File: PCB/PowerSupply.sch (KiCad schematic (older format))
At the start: 21 parts, among them U3 MPM54304

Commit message: Add the FPGA symbol
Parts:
- renumbered C12 to C10, C6 to C4, C7 to C5, C8 to C6, C9 to C7, C10 to C8, C11 to C9, U3 to U2
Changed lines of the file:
@@
 $Descr A4 11693 8268
 encoding utf-8
-Sheet 16 17
+Sheet 15 19
 Title "Litter Robot 3 - Power supply"
 Date "2021-03-02"
@@
 $EndDescr
 $Comp
-L LitterRobot:MPM54304 U3
+L LitterRobot:MPM54304 U2
 U 1 1 60487643
 P 5750 3850
-AR Path="/603F1DCE/60487643" Ref="U3"  Part="1"
+AR Path="/603F1DCE/60487643" Ref="U2"  Part="1"
 AR Path="/60624089/60487643" Ref="U?"  Part="1"
-F 0 "U3" H 5750 6381 50  0000 C CNN
+F 0 "U2" H 5750 6381 50  0000 C CNN
 F 1 "MPM54304" H 5750 3850 100 0000 C CNN
 F 2 "LitterRobot:MPS_MPM54304_LGA33_7x7mm" H 6300 6200 50  0001 C CNN
@@
 $EndComp
 $Comp
-L power:+15V #PWR059
+L power:+15V #PWR052
 U 1 1 6049C802
 P 3900 1500
-AR Path="/603F1DCE/6049C802" Ref="#PWR059"  Part="1"
+AR Path="/603F1DCE/6049C802" Ref="#PWR052"  Part="1"
 AR Path="/60624089/6049C802" Ref="#PWR?"  Part="1"
-F 0 "#PWR059" H 3900 1350 50  0001 C CNN
+F 0 "#PWR052" H 3900 1350 50  0001 C CNN
 F 1 "+15V" H 3915 1673 50  0000 C CNN
 F 2 "" H 3900 1500 50  0001 C CNN
@@
 P 4400 1850
 AR Path="/603F20AB/6049E372" Ref="C?"  Part="1"
-AR Path="/603F1DCE/6049E372" Ref="C7"  Part="1"
+AR Path="/603F1DCE/6049E372" Ref="C5"  Part="1"
 AR Path="/60624089/6049E372" Ref="C?"  Part="1"
-F 0 "C7" H 4515 1941 50  0000 L CNN
+F 0 "C5" H 4515 1941 50  0000 L CNN
 F 1 "22µF" H 4515 1850 50  0000 L CNN
 F 2 "Capacitor_SMD:C_0603_1608Metric" H 4438 1700 50  0001 C CNN
@@
 P 3900 1850
 AR Path="/603F20AB/6049F19A" Ref="C?"  Part="1"
-AR Path="/603F1DCE/6049F19A" Ref="C6"  Part="1"
+AR Path="/603F1DCE/6049F19A" Ref="C4"  Part="1"
 AR Path="/60624089/6049F19A" Ref="C?"  Part="1"
-F 0 "C6" H 4015 1941 50  0000 L CNN
+F 0 "C4" H 4015 1941 50  0000 L CNN
 F 1 "22µF" H 4015 1850 50  0000 L CNN
 F 2 "Capacitor_SMD:C_0603_1608Metric" H 3938 1700 50  0001 C CNN
@@
 $EndComp
 $Comp
-L power:GND #PWR060
+L power:GND #PWR053
 U 1 1 604A0BB2
 P 4400 2200
-AR Path="/603F1DCE/604A0BB2" Ref="#PWR060"  Part="1"
+AR Path="/603F1DCE/604A0BB2" Ref="#PWR053"  Part="1"
 AR Path="/60624089/604A0BB2" Ref="#PWR?"  Part="1"
-F 0 "#PWR060" H 4400 1950 50  0001 C CNN
+F 0 "#PWR053" H 4400 1950 50  0001 C CNN
 F 1 "GND" H 4405 2027 50  0000 C CNN
 F 2 "" H 4400 2200 50  0001 C CNN
@@
 $EndComp
 $Comp
-L power:GND #PWR061
+L power:GND #PWR054
 U 1 1 604A378F
 P 4400 3500
-AR Path="/603F1DCE/604A378F" Ref="#PWR061"  Part="1"
+AR Path="/603F1DCE/604A378F" Ref="#PWR054"  Part="1"
 AR Path="/60624089/604A378F" Ref="#PWR?"  Part="1"
-F 0 "#PWR061" H 4400 3250 50  0001 C CNN
+F 0 "#PWR054" H 4400 3250 50  0001 C CNN
 F 1 "GND" H 4405 3327 50  0000 C CNN
 F 2 "" H 4400 3500 50  0001 C CNN
@@
 $EndComp
 $Comp
-L power:GND #PWR063
+L power:GND #PWR056
 U 1 1 604A4E38
 P 4400 5400
-AR Path="/603F1DCE/604A4E38" Ref="#PWR063"  Part="1"
+AR Path="/603F1DCE/604A4E38" Ref="#PWR056"  Part="1"
 AR Path="/60624089/604A4E38" Ref="#PWR?"  Part="1"
-F 0 "#PWR063" H 4400 5150 50  0001 C CNN
+F 0 "#PWR056" H 4400 5150 50  0001 C CNN
 F 1 "GND" H 4405 5227 50  0000 C CNN
 F 2 "" H 4400 5400 50  0001 C CNN
@@
 $EndComp
 $Comp
-L power:+15V #PWR062
+L power:+15V #PWR055
 U 1 1 604A52BA
 P 4400 4400
-AR Path="/603F1DCE/604A52BA" Ref="#PWR062"  Part="1"
+AR Path="/603F1DCE/604A52BA" Ref="#PWR055"  Part="1"
 AR Path="/60624089/604A52BA" Ref="#PWR?"  Part="1"
-F 0 "#PWR062" H 4400 4250 50  0001 C CNN
+F 0 "#PWR055" H 4400 4250 50  0001 C CNN
 F 1 "+15V" H 4415 4573 50  0000 C CNN
 F 2 "" H 4400 4400 50  0001 C CNN
@@
 P 5500 6550
 AR Path="/603F20AB/604AB97B" Ref="C?"  Part="1"
-AR Path="/603F1DCE/604AB97B" Ref="C8"  Part="1"
+AR Path="/603F1DCE/604AB97B" Ref="C6"  Part="1"
 AR Path="/60624089/604AB97B" Ref="C?"  Part="1"
-F 0 "C8" H 5615 6641 50  0000 L CNN
+F 0 "C6" H 5615 6641 50  0000 L CNN
 F 1 "1µF" H 5615 6550 50  0000 L CNN
 F 2 "Capacitor_SMD:C_0603_1608Metric" H 5538 6400 50  0001 C CNN
@@
 $EndComp
 $Comp
-L power:GND #PWR064
+L power:GND #PWR057
 U 1 1 604AC677
 P 6000 6900
-AR Path="/603F1DCE/604AC677" Ref="#PWR064"  Part="1"
+AR Path="/603F1DCE/604AC677" Ref="#PWR057"  Part="1"
 AR Path="/60624089/604AC677" Ref="#PWR?"  Part="1"
-F 0 "#PWR064" H 6000 6650 50  0001 C CNN
+F 0 "#PWR057" H 6000 6650 50  0001 C CNN
 F 1 "GND" H 6005 6727 50  0000 C CNN
 F 2 "" H 6000 6900 50  0001 C CNN
@@
 $EndComp
 $Comp
-L LitterRobot:+7V #PWR069
+L LitterRobot:+7V #PWR062
 U 1 1 604AE53B
 P 7900 1500
-AR Path="/603F1DCE/604AE53B" Ref="#PWR069"  Part="1"
+AR Path="/603F1DCE/604AE53B" Ref="#PWR062"  Part="1"
 AR Path="/60624089/604AE53B" Ref="#PWR?"  Part="1"
-F 0 "#PWR069" H 7900 1350 50  0001 C CNN
+F 0 "#PWR062" H 7900 1350 50  0001 C CNN
 F 1 "+7V" H 7915 1673 50  0000 C CNN
 F 2 "" H 7900 1500 50  0001 C CNN
@@
 $EndComp
 $Comp
-L power:+2V5 #PWR071
+L power:+2V5 #PWR064
 U 1 1 604B00EC
 P 7900 3700
-AR Path="/603F1DCE/604B00EC" Ref="#PWR071"  Part="1"
+AR Path="/603F1DCE/604B00EC" Ref="#PWR064"  Part="1"
 AR Path="/60624089/604B00EC" Ref="#PWR?"  Part="1"
-F 0 "#PWR071" H 7900 3550 50  0001 C CNN
+F 0 "#PWR064" H 7900 3550 50  0001 C CNN
 F 1 "+2V5" H 7915 3873 50  0000 C CNN
 F 2 "" H 7900 3700 50  0001 C CNN
@@
 $EndComp
 $Comp
-L power:+1V2 #PWR072
+L power:+1V2 #PWR065
 U 1 1 604B0B68
 P 7900 4800
-AR Path="/603F1DCE/604B0B68" Ref="#PWR072"  Part="1"
+AR Path="/603F1DCE/604B0B68" Ref="#PWR065"  Part="1"
 AR Path="/60624089/604B0B68" Ref="#PWR?"  Part="1"
-F 0 "#PWR072" H 7900 4650 50  0001 C CNN
+F 0 "#PWR065" H 7900 4650 50  0001 C CNN
 F 1 "+1V2" H 7915 4973 50  0000 C CNN
 F 2 "" H 7900 4800 50  0001 C CNN
@@
 $EndComp
 $Comp
-L power:GND #PWR065
+L power:GND #PWR058
 U 1 1 604B58A1
 P 6900 2450
-AR Path="/603F1DCE/604B58A1" Ref="#PWR065"  Part="1"
+AR Path="/603F1DCE/604B58A1" Ref="#PWR058"  Part="1"
 AR Path="/60624089/604B58A1" Ref="#PWR?"  Part="1"
-F 0 "#PWR065" H 6900 2200 50  0001 C CNN
+F 0 "#PWR058" H 6900 2200 50  0001 C CNN
 F 1 "GND" H 6905 2277 50  0000 C CNN
 F 2 "" H 6900 2450 50  0001 C CNN
@@
 P 7400 2000
 AR Path="/603F20AB/604C9334" Ref="C?"  Part="1"
-AR Path="/603F1DCE/604C9334" Ref="C9"  Part="1"
+AR Path="/603F1DCE/604C9334" Ref="C7"  Part="1"
 AR Path="/60624089/604C9334" Ref="C?"  Part="1"
-F 0 "C9" H 7515 2091 50  0000 L CNN
+F 0 "C7" H 7515 2091 50  0000 L CNN
 F 1 "22µF" H 7515 2000 50  0000 L CNN
 F 2 "Capacitor_SMD:C_0603_1608Metric" H 7438 1850 50  0001 C CNN
@@
 $EndComp
 $Comp
-L power:GND #PWR066
+L power:GND #PWR059
 U 1 1 604CD969
 P 6900 3550
-AR Path="/603F1DCE/604CD969" Ref="#PWR066"  Part="1"
+AR Path="/603F1DCE/604CD969" Ref="#PWR059"  Part="1"
 AR Path="/60624089/604CD969" Ref="#PWR?"  Part="1"
-F 0 "#PWR066" H 6900 3300 50  0001 C CNN
+F 0 "#PWR059" H 6900 3300 50  0001 C CNN
 F 1 "GND" H 6905 3377 50  0000 C CNN
 F 2 "" H 6900 3550 50  0001 C CNN
@@
 P 7400 3100
 AR Path="/603F20AB/604CD971" Ref="C?"  Part="1"
-AR Path="/603F1DCE/604CD971" Ref="C10"  Part="1"
+AR Path="/603F1DCE/604CD971" Ref="C8"  Part="1"
 AR Path="/60624089/604CD971" Ref="C?"  Part="1"
-F 0 "C10" H 7515 3191 50  0000 L CNN
+F 0 "C8" H 7515 3191 50  0000 L CNN
 F 1 "22µF" H 7515 3100 50  0000 L CNN
 F 2 "Capacitor_SMD:C_0603_1608Metric" H 7438 2950 50  0001 C CNN
@@
 $EndComp
 $Comp
-L power:GND #PWR067
+L power:GND #PWR060
 U 1 1 604D130C
 P 6900 4650
-AR Path="/603F1DCE/604D130C" Ref="#PWR067"  Part="1"
+AR Path="/603F1DCE/604D130C" Ref="#PWR060"  Part="1"
 AR Path="/60624089/604D130C" Ref="#PWR?"  Part="1"
-F 0 "#PWR067" H 6900 4400 50  0001 C CNN
+F 0 "#PWR060" H 6900 4400 50  0001 C CNN
 F 1 "GND" H 6905 4477 50  0000 C CNN
 F 2 "" H 6900 4650 50  0001 C CNN
@@
 P 7400 4200
 AR Path="/603F20AB/604D1314" Ref="C?"  Part="1"
-AR Path="/603F1DCE/604D1314" Ref="C11"  Part="1"
+AR Path="/603F1DCE/604D1314" Ref="C9"  Part="1"
 AR Path="/60624089/604D1314" Ref="C?"  Part="1"
-F 0 "C11" H 7515 4291 50  0000 L CNN
+F 0 "C9" H 7515 4291 50  0000 L CNN
 F 1 "22µF" H 7515 4200 50  0000 L CNN
 F 2 "Capacitor_SMD:C_0603_1608Metric" H 7438 4050 50  0001 C CNN
@@
 	7900 4900 7400 4900
 $Comp
-L power:GND #PWR068
+L power:GND #PWR061
 U 1 1 604D31B7
 P 6900 5750
-AR Path="/603F1DCE/604D31B7" Ref="#PWR068"  Part="1"
+AR Path="/603F1DCE/604D31B7" Ref="#PWR061"  Part="1"
 AR Path="/60624089/604D31B7" Ref="#PWR?"  Part="1"
-F 0 "#PWR068" H 6900 5500 50  0001 C CNN
+F 0 "#PWR061" H 6900 5500 50  0001 C CNN
 F 1 "GND" H 6905 5577 50  0000 C CNN
 F 2 "" H 6900 5750 50  0001 C CNN
@@
 P 7400 5300
 AR Path="/603F20AB/604D31BF" Ref="C?"  Part="1"
-AR Path="/603F1DCE/604D31BF" Ref="C12"  Part="1"
+AR Path="/603F1DCE/604D31BF" Ref="C10"  Part="1"
 AR Path="/60624089/604D31BF" Ref="C?"  Part="1"
-F 0 "C12" H 7515 5391 50  0000 L CNN
+F 0 "C10" H 7515 5391 50  0000 L CNN
 F 1 "22µF" H 7515 5300 50  0000 L CNN
 F 2 "Capacitor_SMD:C_0603_1608Metric" H 7438 5150 50  0001 C CNN
@@
 	4400 1600 4900 1600
 $Comp
-L power:+3V3 #PWR070
+L power:+3V3 #PWR063
 U 1 1 604F7C44
 P 7900 2600
-AR Path="/603F1DCE/604F7C44" Ref="#PWR070"  Part="1"
+AR Path="/603F1DCE/604F7C44" Ref="#PWR063"  Part="1"
 AR Path="/60624089/604F7C44" Ref="#PWR?"  Part="1"
-F 0 "#PWR070" H 7900 2450 50  0001 C CNN
+F 0 "#PWR063" H 7900 2450 50  0001 C CNN
 F 1 "+3V3" H 7915 2773 50  0000 C CNN
 F 2 "" H 7900 2600 50  0001 C CNN
@@
 $EndComp
 $Comp
-L power:+3V3 #PWR073
+L power:+3V3 #PWR066
 U 1 1 6057D204
 P 8500 5400
-AR Path="/603F1DCE/6057D204" Ref="#PWR073"  Part="1"
+AR Path="/603F1DCE/6057D204" Ref="#PWR066"  Part="1"
 AR Path="/60624089/6057D204" Ref="#PWR?"  Part="1"
-F 0 "#PWR073" H 8500 5250 50  0001 C CNN
+F 0 "#PWR066" H 8500 5250 50  0001 C CNN
 F 1 "+3V3" H 8515 5573 50  0000 C CNN
 F 2 "" H 8500 5400 50  0001 C CNN

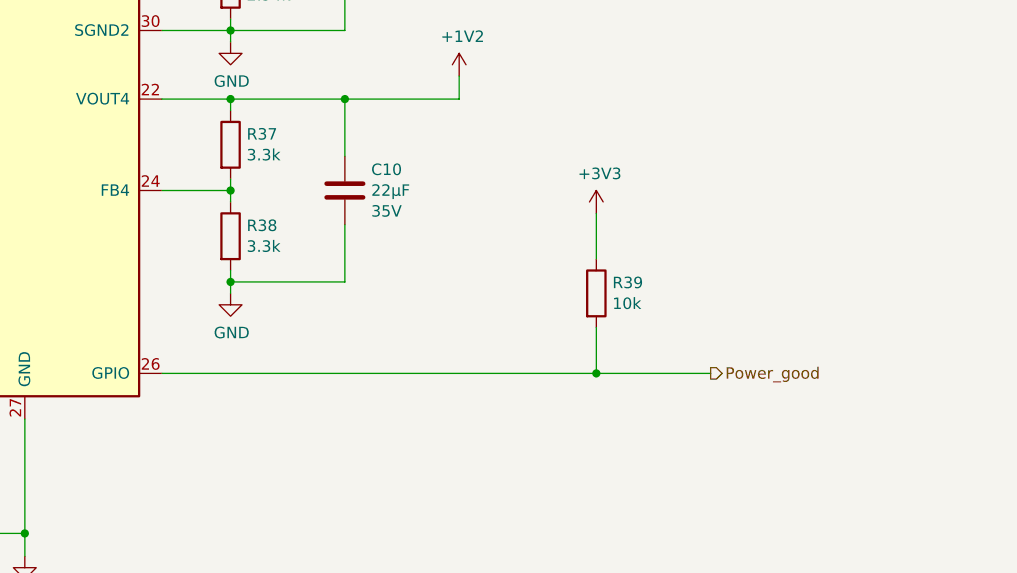
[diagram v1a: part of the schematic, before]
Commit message: Connect the FPGA configuration signals
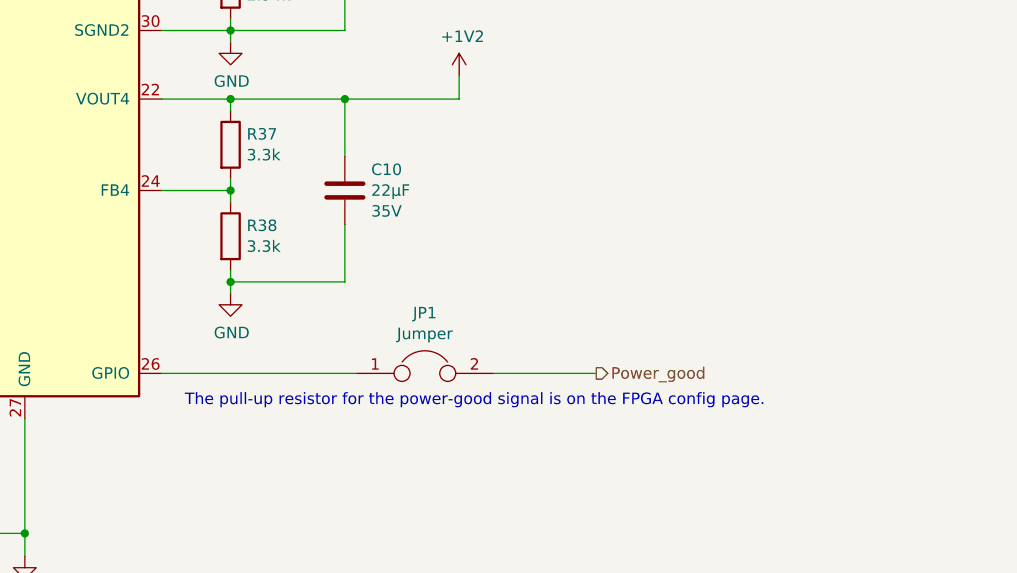
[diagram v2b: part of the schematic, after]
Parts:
- removed R39: 10k, Resistor_SMD:R_0603_1608Metric, symbol Device:R
- added JP1: Jumper, Jumper:SolderJumper-2_P1.3mm_Bridged_RoundedPad1.0x1.5mm, symbol Device:Jumper
- C10, C4, C5, C7, C8, C9: Part_Number C3216X5R1V226M160AC -> (none); Part_number (none) -> C3216X5R1V226M160AC
- C6: Part_Number C1608X5R1H105K080AB -> (none); Part_number (none) -> C1608X5R1H105K080AB
- R27, R28, R29: Part_Number CR0603-FX-1002ELF -> (none); Part_number (none) -> CR0603-FX-1002ELF
- R30, R37, R38: Part_Number CR0603-FX-3301ELF -> (none); Part_number (none) -> CR0603-FX-3301ELF
- R31: Part_Number CR0603-FX-2002ELF -> (none); Part_number (none) -> CR0603-FX-2002ELF
- R32: Part_Number CR0603-FX-1871ELF -> (none); Part_number (none) -> CR0603-FX-1871ELF
- R33: Part_Number CR0603-FX-1152ELF -> (none); Part_number (none) -> CR0603-FX-1152ELF
- R34: Part_Number CR0603-FX-2551ELF -> (none); Part_number (none) -> CR0603-FX-2551ELF
- R35: Part_Number CR0603-FX-9311ELF -> (none); Part_number (none) -> CR0603-FX-9311ELF
- R36: Part_Number CR0603-FX-2941ELF -> (none); Part_number (none) -> CR0603-FX-2941ELF
- U2: Part_Number MPM54304GMN-0001 -> (none); Part_number (none) -> MPM54304GMN-0001
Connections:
- net Power_good: now also JP1.2; no longer U2.26 (GPIO)
- new net: JP1.1, U2.26 (GPIO)
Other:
- note added: "The pull-up resistor for the power-good signal is on the FPGA config page."
